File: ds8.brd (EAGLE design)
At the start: 85 x 50 mm, 93 parts, among them IC1 TM4C1230C3PM, IC2 TPS77333, Q1 BC850, Q2 BC850, Q3 BC850, U1 LM13700M, U2 LM324, U3 LM324, U4 LM741D, X1 MAB5SH

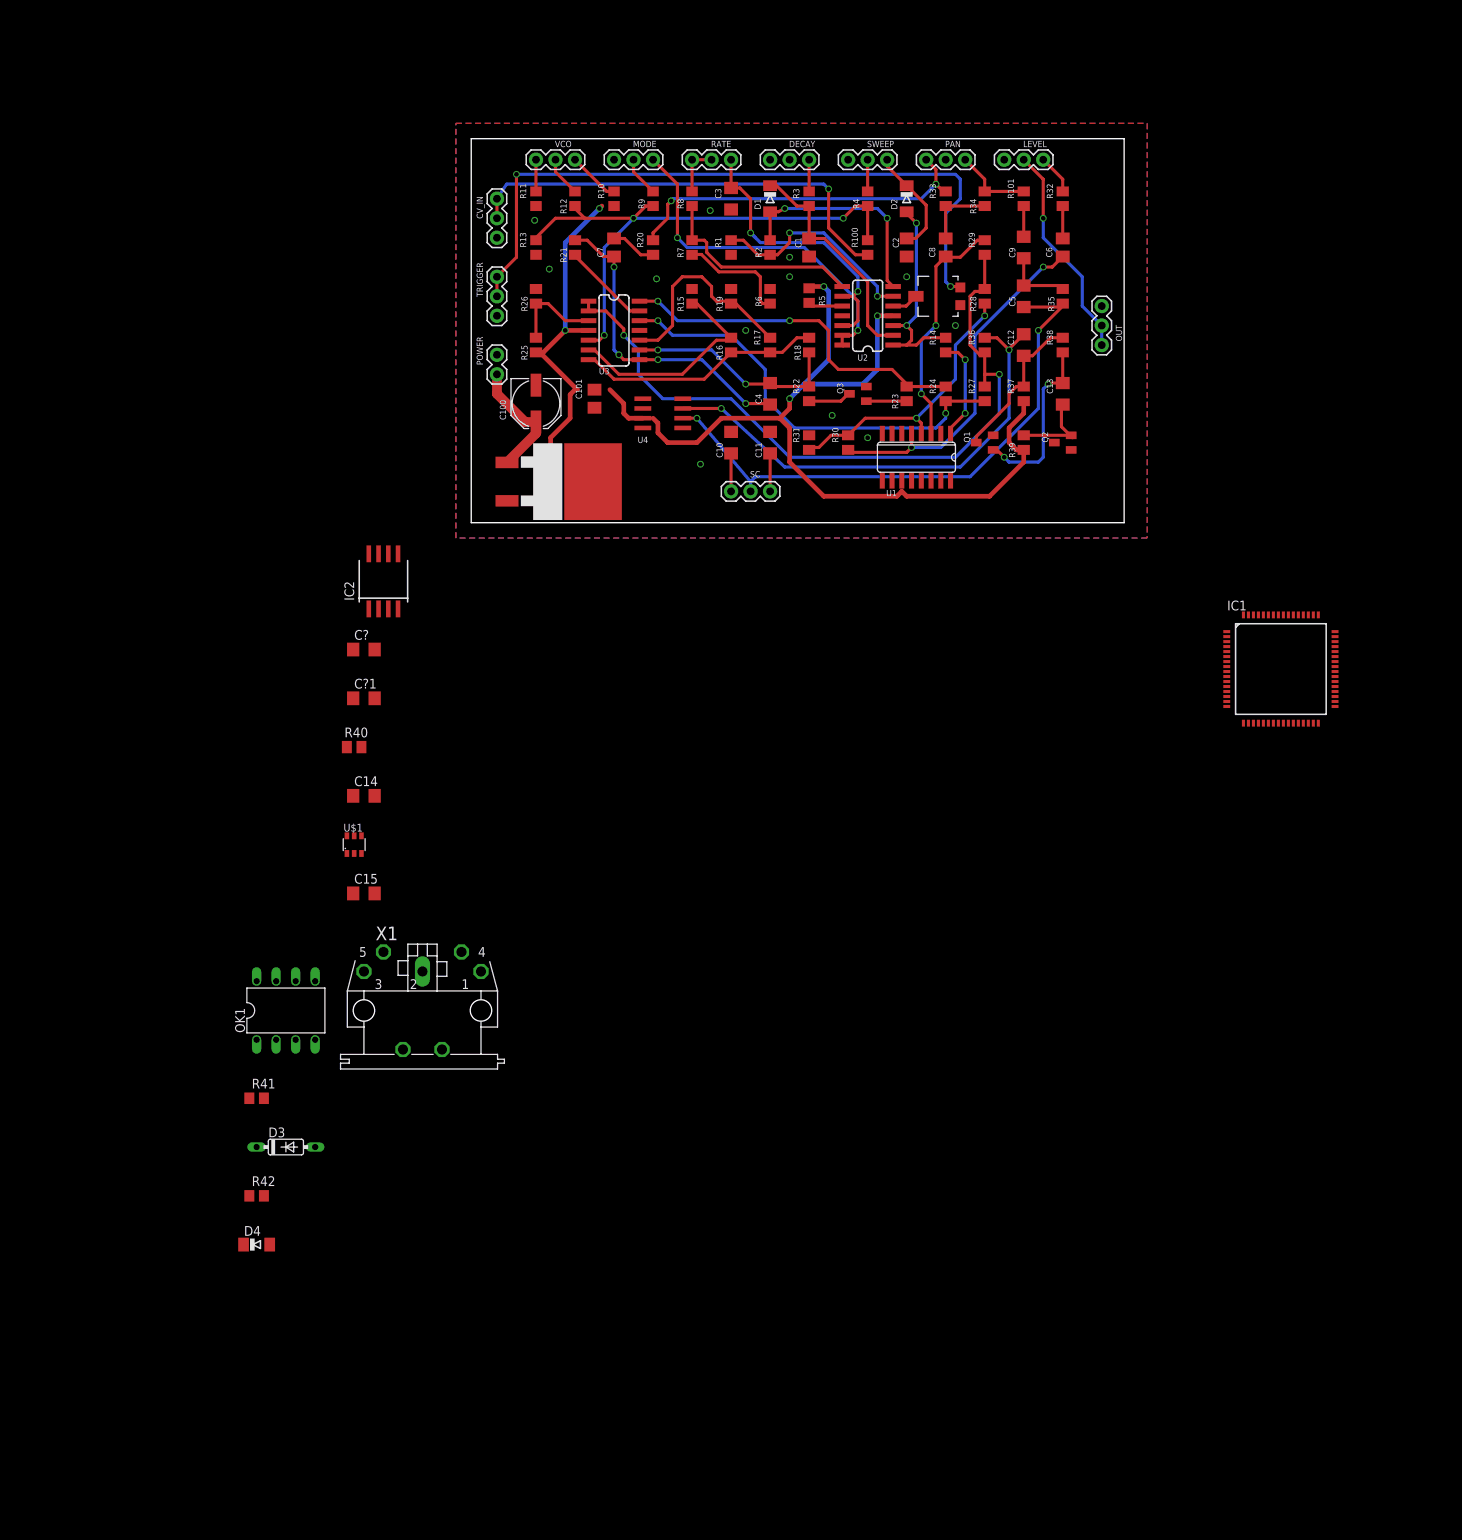
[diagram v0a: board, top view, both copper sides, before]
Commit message: Board retouted
- Cleaned the schematic
- Board rerouted with through hole pots and new connectors
- Lots of little stuff

Signed-off-by: Kamel Makhloufi <melka@blaste.net>
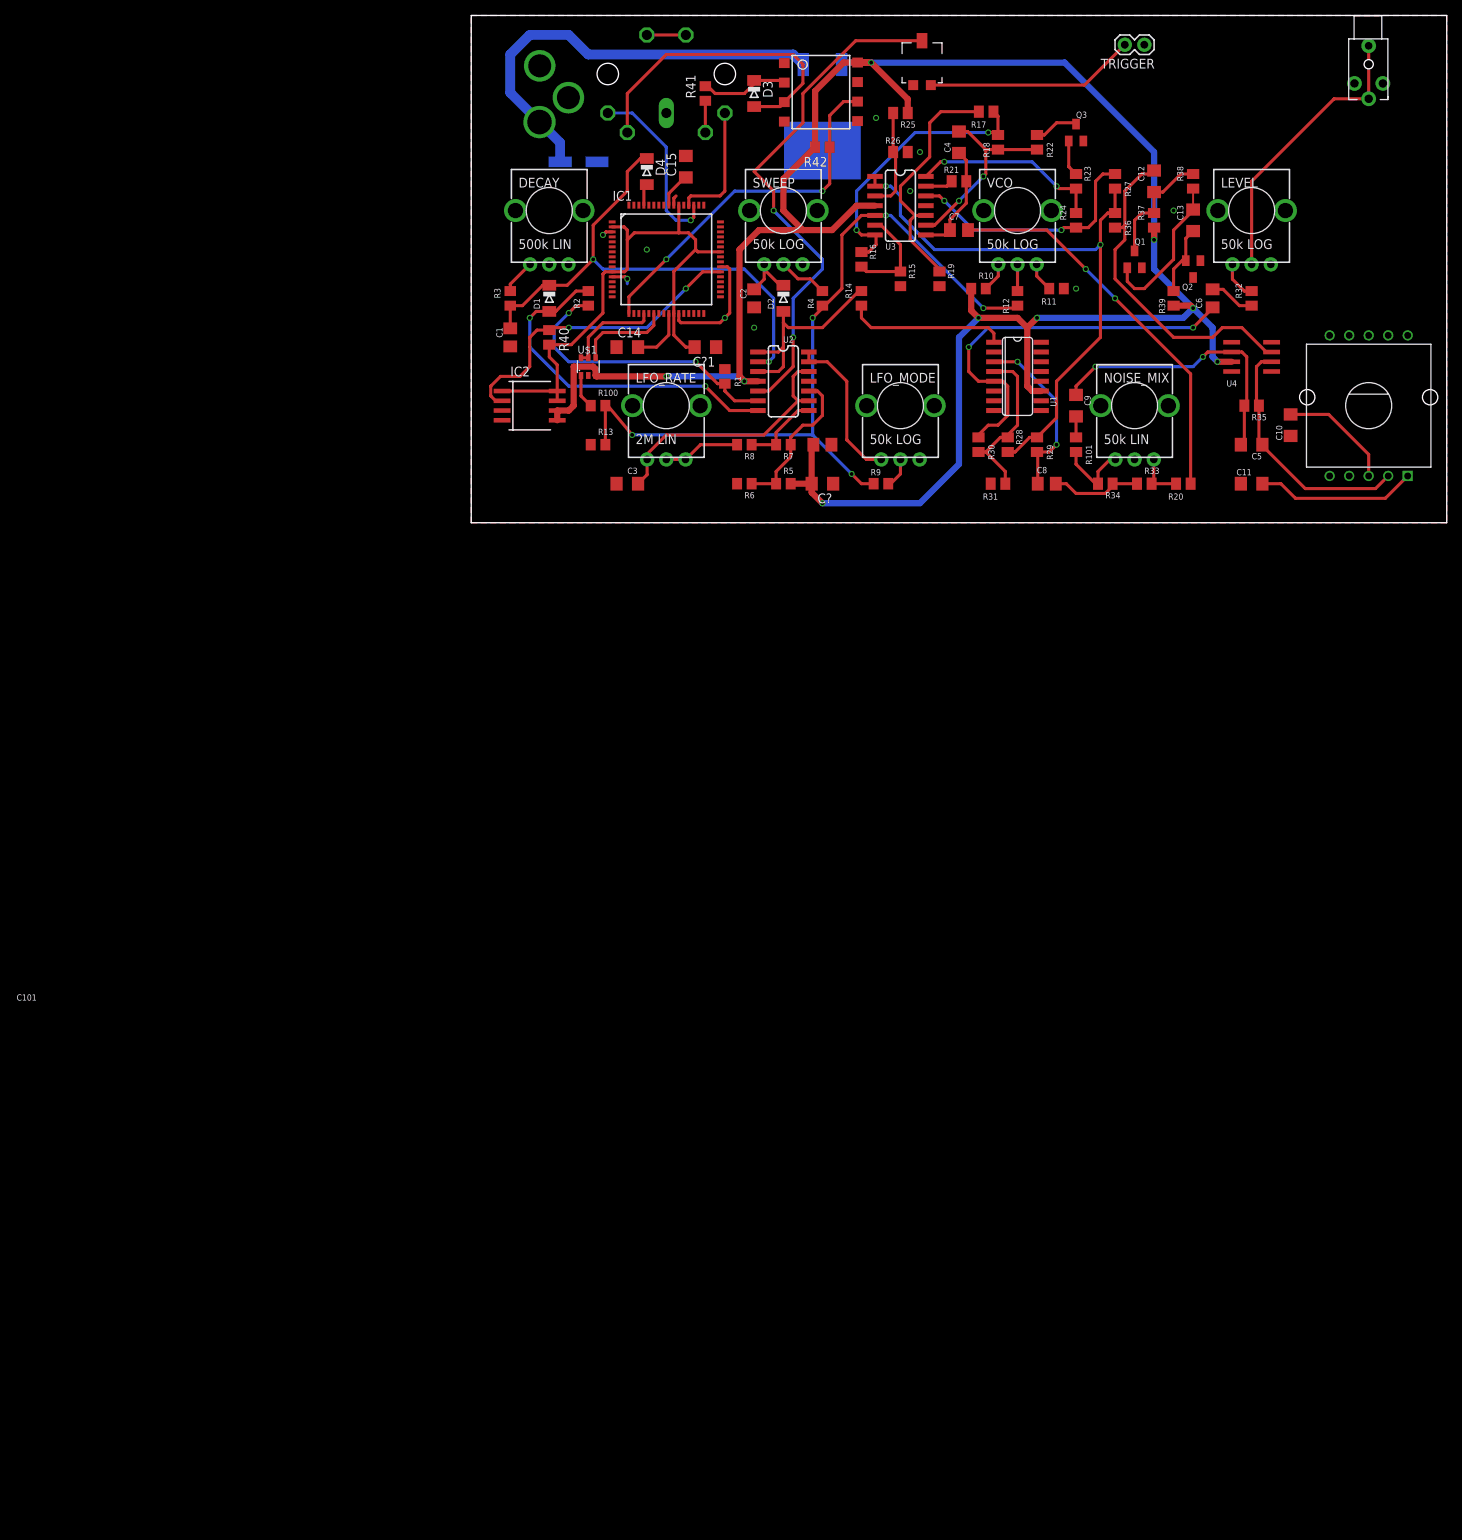
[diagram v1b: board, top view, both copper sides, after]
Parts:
- removed CV_IN, OUT: 3.5 JACK, SparkFun-Connectors:1X03
- removed MODE: 50K LOG, SparkFun-Connectors:1X03
- removed OK1: 6N138, optocoupler:DIL08
- removed PAN: 50K LIN, SparkFun-Connectors:1X03
- removed POWER: 9V, SparkFun-Connectors:1X02
- removed RATE: 2M LIN, SparkFun-Connectors:1X03
- removed SC: ROCKER_SWITCH, SparkFun-Connectors:1X03
- added J1: 9VDC, SparkFun-Connectors:POWER_JACK_PTH_LOCK
- added JP1: (no value), SparkFun-Connectors:STEREOJACK2.5MM_STEREOJACK2.5MM
- added LFO_MODE: 50k LOG, SparkFun-Electromechanical:ALPS_POT_KIT
- added LFO_RATE: 2M LIN, SparkFun-Electromechanical:ALPS_POT_KIT
- added NOISE_MIX: 50k LIN, SparkFun-Electromechanical:ALPS_POT_KIT
- added U$3: ALPS_SRBV, ds8:ALPS_SRBV
- added U$4: OPTO_DARL_6N138S, SparkFun-DiscreteSemi:8-SMD
- D3: value 1N4148DO35-7 -> 4148; device diode:DO35-7 -> diode:MINIMELF
- DECAY: value 500K LIN -> 500k LIN; device SparkFun-Connectors:1X03 -> SparkFun-Electromechanical:ALPS_POT_KIT
- LEVEL, SWEEP, VCO: value 50K LOG -> 50k LOG; device SparkFun-Connectors:1X03 -> SparkFun-Electromechanical:ALPS_POT_KIT
- TRIGGER: value 3.5 JACK -> M02PTH; device SparkFun-Connectors:1X03 -> SparkFun-Connectors:1X02
- moved R42 155.1 mm to (45.7, 48.9), turned to 180 degrees
- moved D3 150.1 mm to (36.8, 55.9), turned to 270 degrees
- moved D4 148.6 mm to (22.9, 45.7), turned to 270 degrees
- moved R41 143.3 mm to (30.5, 55.9), turned to 90 degrees
- moved X1 126.0 mm to (25.4, 58.4), flipped to the bottom, turned to 180 degrees
- moved C15 103.5 mm to (27.9, 46.4), turned to 90 degrees
- moved IC1 96.2 mm to (25.4, 34.3)
- moved TRIGGER 91.4 mm to (87.6, 62.2), turned to 180 degrees
- moved U4 77.0 mm to (101.6, 21.6)
- moved R20 75.6 mm to (92.7, 5.08), turned to 180 degrees
- moved C10 72.9 mm to (106.7, 12.7)
- moved U$1 69.3 mm to (15.2, 20.3)
- moved R11 68.8 mm to (76.2, 30.5), turned to 180 degrees
- moved C14 67.7 mm to (20.3, 22.9)
- moved U$2 64.6 mm to (45.7, 57.1), flipped to the bottom, turned to 180 degrees
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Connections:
- net N$34 renamed TRIGGER
- removed net PAN1: PAN.1, R20.2, R33.2
- removed net PAN2: PAN.2
- removed net PAN3: PAN.3, R101.2, R34.1
- removed net SC1: C10.2, SC.1
- removed net SC2: C5.2, R35.2, SC.2, U4.2
- removed net SC3: C11.2, SC.3
- removed net TRIG: RV1.A, TRIGGER.2, TRIGGER.3
- removed net VCO1: R11.2, VCO.1
- removed net VCO3: R10.2, VCO.3
- new net N$34: RV1.A, TRIGGER.2
- new net N$37: R10.2, VCO.P$1
- new net N$38: R11.2, VCO.P$3
- new net N$39: C10.1, U$3.P$3
- new net N$40: C11.1, U$3.P$1
- new net NOISECOLOR_2: C5.2, R35.2, U$3.P$2, U4.2
- new net NOISEMIX_1: NOISE_MIX.P$3, R20.2, R33.2
- new net NOISEMIX_3: NOISE_MIX.P$1, R101.2, R34.1
- net /RESET: now also R40.1; no longer R40.2
- net 9VDC: now also J1.PWR; no longer POWER.1
- net CVIN: no longer CV_IN.2, CV_IN.3
- net DECAY: now also DECAY.P$1; no longer DECAY.3
- net GND: now also C10.2, C11.2, C15.2, DECAY.P$2, DECAY.P$3, J1.GND, J1.GNDBREAK, JP1.RING1, LEVEL.P$3, LFO_MODE.P$3, NOISE_MIX.P$2, SWEEP.P$3, U$4.5; no longer C10.1, C11.1, C15.1, CV_IN.1, DECAY.1, DECAY.2, LEVEL.1, MODE.1, OK1.5, OUT.1, POWER.2, SWEEP.1
- net LFO2: now also LFO_MODE.P$2; no longer MODE.2
- net LFO3: now also LFO_MODE.P$1; no longer MODE.3
- net MIDI_IN: now also U$4.6; no longer OK1.6
- net N$26: now also U$4.2; no longer OK1.2
- net N$28: now also U4.6
- net N$35: now also U$4.3; no longer OK1.3
- net N$36: now also C15.1; no longer C15.2
- net N$5: now also R5.1
- net N$57: now also JP1.SHIELD, JP1.TIP, LEVEL.P$2; no longer LEVEL.2, OUT.2, OUT.3
- net OUT: now also LEVEL.P$1; no longer LEVEL.3
- net S2: now also LFO_RATE.P$1; no longer RATE.3
- net S3: now also LFO_RATE.P$2, LFO_RATE.P$3; no longer RATE.1, RATE.2
- net SWEEP2: now also SWEEP.P$2; no longer SWEEP.2
- net SWEEP3: now also SWEEP.P$1; no longer SWEEP.3
- net VCC: now also U$4.8; no longer OK1.8
- net VCO2: now also VCO.P$2; no longer VCO.2
- net VDD: now also R40.2; no longer R40.1
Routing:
- net VCC: track 166.9 -> 288.3 mm, vias 5 -> 9
- net TRIG: track 91.3 -> 0.00 mm, vias 2 -> 0
- net SC2: track 75.6 -> 0.00 mm, vias 2 -> 0
- net VDD: track 0.00 -> 72.9 mm
- net TRIGGER: track 3.50 -> 67.7 mm, vias 0 -> 2
- net CVIN: track 58.6 -> 4.46 mm, vias 1 -> 0
- net MIDI_IN: track 0.00 -> 47.7 mm, vias 0 -> 2
- net PAN1: track 47.2 -> 0.00 mm, vias 2 -> 0
- net N$13: track 5.96 -> 51.0 mm, vias 0 -> 2
- net 9VDC: track 16.0 -> 57.4 mm
- net /RESET: track 0.00 -> 41.3 mm, vias 0 -> 2
- net N$35: track 0.00 -> 40.7 mm
- net N$3: track 29.9 -> 68.3 mm, vias 0 -> 2
- net NOISECOLOR_2: track 0.00 -> 32.2 mm
- net N$28: track 8.82 -> 37.2 mm, vias 0 -> 2
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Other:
- board size 85 x 50 mm -> 127 x 66 mm

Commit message: added more decoupling to vdd pins. jtag in place with a reset line
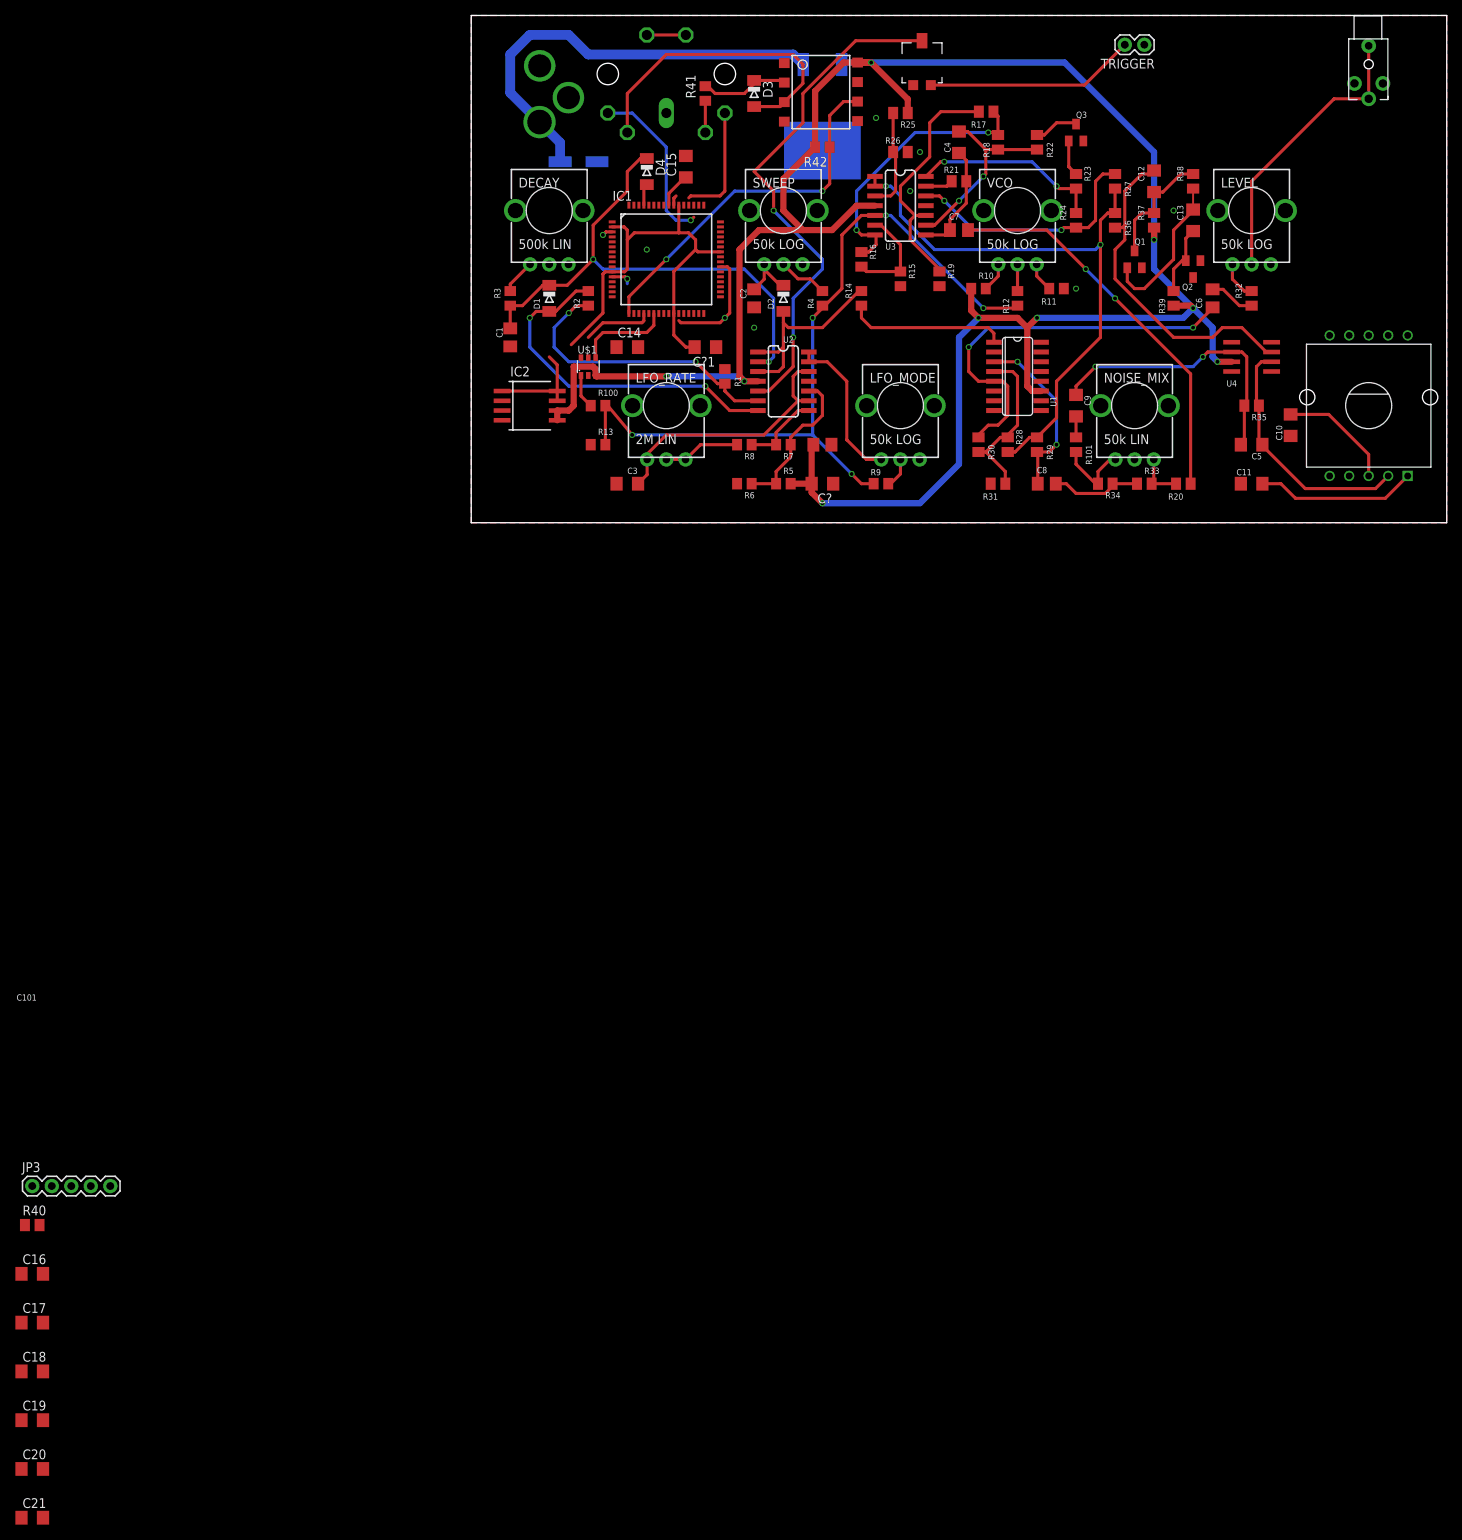
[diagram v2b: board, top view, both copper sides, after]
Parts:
- added C16, C17, C18, C19, C20, C21: 0.01uF, rcl:C1206
- added JP3: (no value), SparkFun-Connectors:1X05
- moved R40 133.7 mm to (-57.1, -91.4), turned to 0 degrees
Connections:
- removed net /RESET: IC1.38, IC2.2, R40.1
- new net N$41: IC1.38, JP3.5, R40.1
- new net N$42: C21.2, IC1.25
- new net TCK: IC1.52, JP3.1
- new net TDI: IC1.50, JP3.4
- new net TDO: IC1.49, JP3.3
- new net TMS: IC1.51, JP3.2
- net ARM_SSI0_FS: no longer U$1.5
- net GND: now also C16.1, C17.2, C18.1, C19.1, C20.1, C21.1
- net N$6: now also U$1.5; no longer C14.2, IC1.25
- net SWCLK: no longer IC1.52
- net SWDIO: no longer IC1.51
- net VDD: now also C14.2, C16.2, C17.1, C18.2, C19.2, C20.2
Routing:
- net /RESET: track 41.3 -> 0.00 mm, vias 2 -> 0
- net N$6: track 7.45 -> 0.00 mm
- net VDD: track 72.9 -> 68.4 mm
- net ARM_SSI0_FS: track 12.7 -> 9.08 mm
- net SWDIO: track 23.6 -> 22.0 mm
- net SWCLK: track 16.5 -> 15.2 mm
- net GND: track 20.7 -> 19.7 mm
